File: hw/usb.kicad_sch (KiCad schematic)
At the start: 12 parts, among them J1001 USB_C_Receptacle_USB2.0_14P, Q1001 CSD18543Q3A, U1001 TPD4S480RUKR, U1002 TPS26750SRSMR

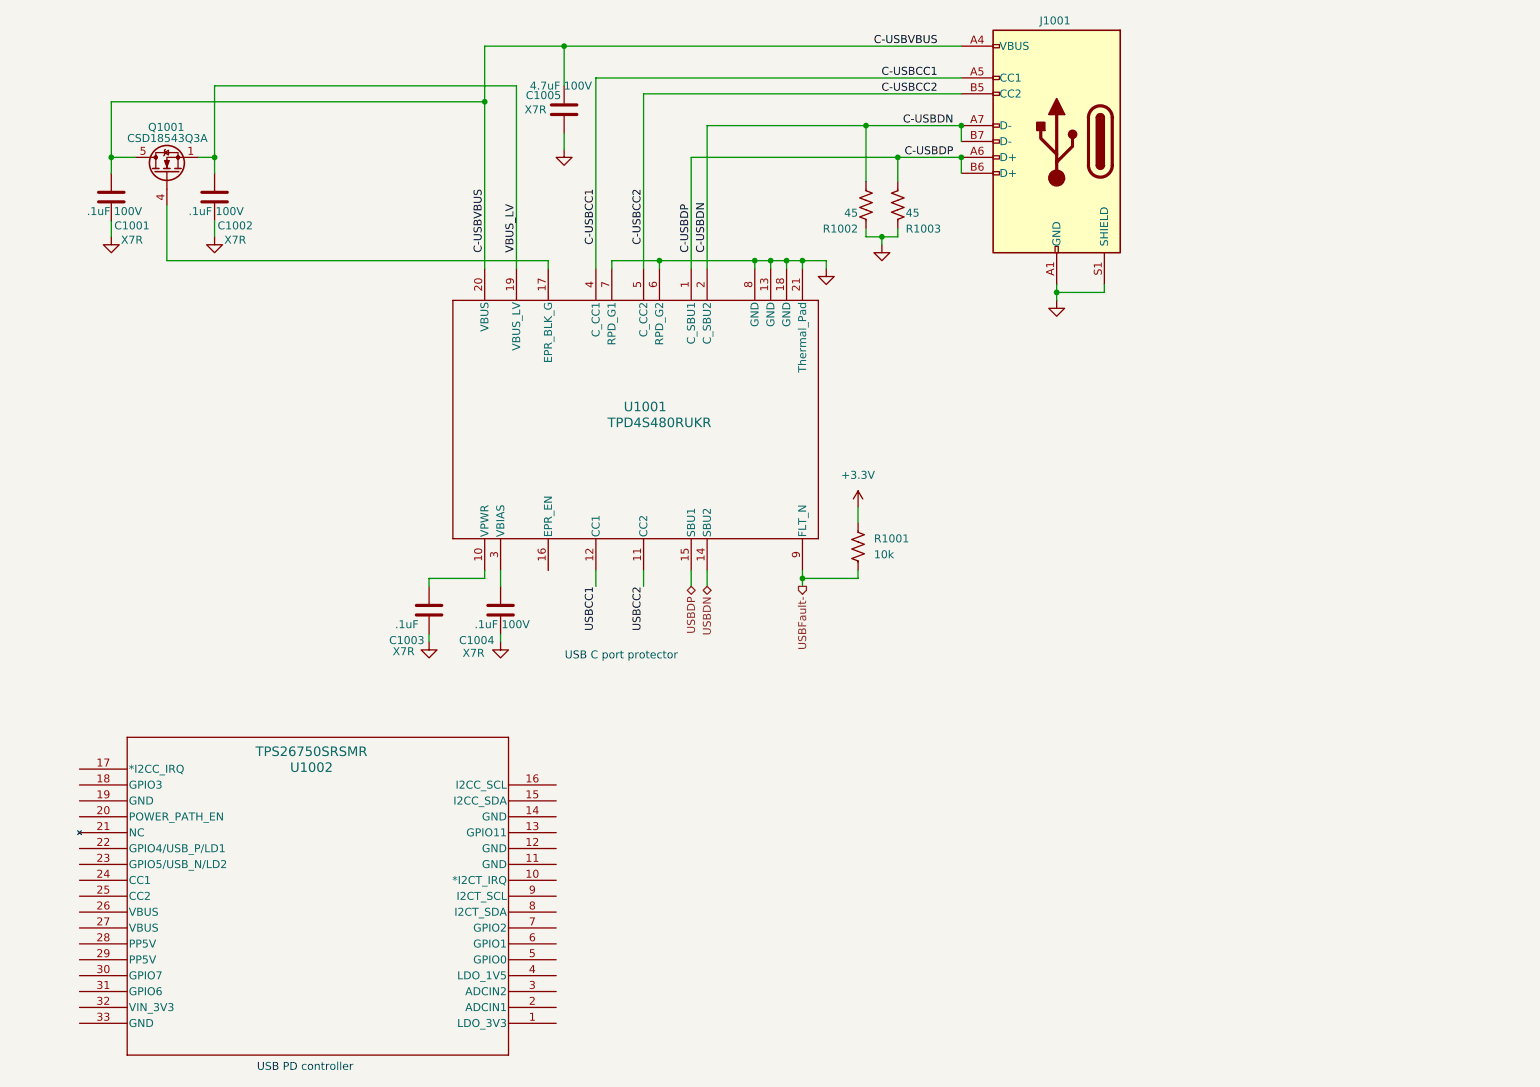
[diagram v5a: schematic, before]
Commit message: Tx LPF and its selection is pretty much done. Fix some OCD. Start to describe the design and construction.
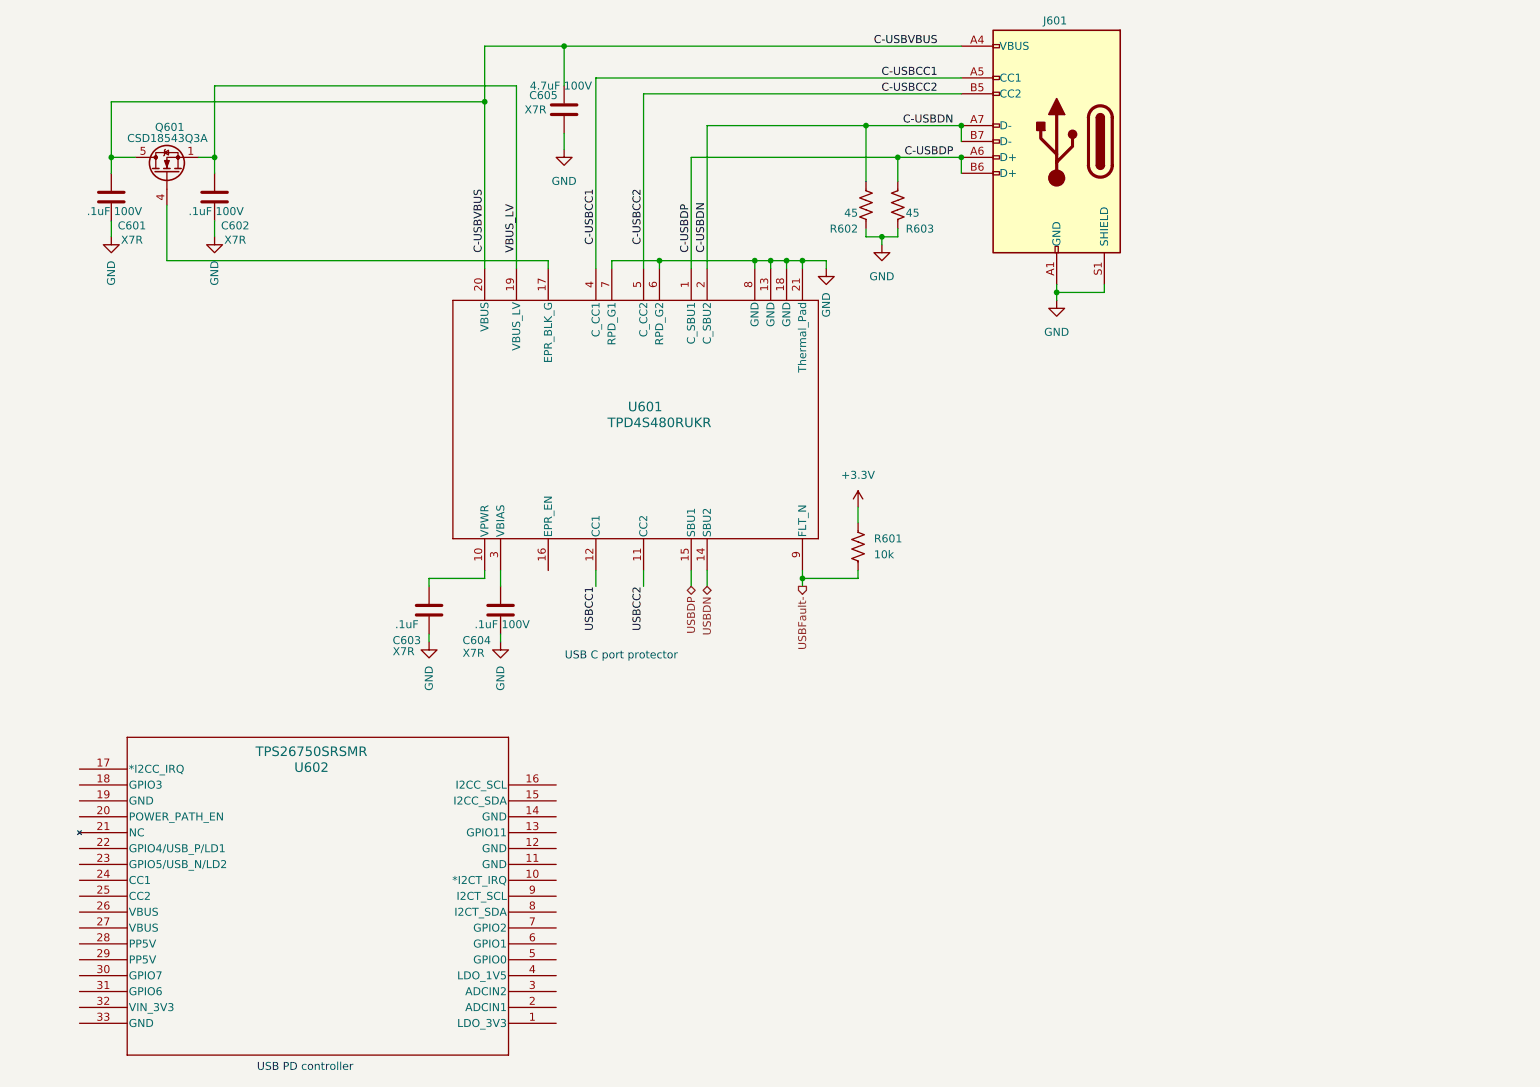
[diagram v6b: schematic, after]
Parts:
- renumbered C1001 to C601, C1002 to C602, C1003 to C603, C1004 to C604, C1005 to C605, J1001 to J601, Q1001 to Q601, R1001 to R601, R1002 to R602, R1003 to R603, U1001 to U601, U1002 to U602
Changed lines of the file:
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@@
 		(on_board yes)
 		(dnp no)
-		(property "Reference" "U1001"
+		(property "Reference" "U601"
 			(at 125.984 84.328 90)
 			(effects
@@
 			(project "USB-SSB-txcvr"
 				(path "/8ae46c04-d01a-4756-8774-512b694bfaff/989674b0-a935-4352-9502-d92e0c9bb54e"
-					(reference "U1001")
+					(reference "U601")
 					(unit 1)
 				)
@@
 		(on_board yes)
 		(dnp no)
-		(property "Reference" "R1003"
+		(property "Reference" "R603"
 			(at 167.64 55.88 0)
 			(effects
@@
 			(project "USB-SSB-txcvr"
 				(path "/8ae46c04-d01a-4756-8774-512b694bfaff/989674b0-a935-4352-9502-d92e0c9bb54e"
-					(reference "R1003")
+					(reference "R603")
 					(unit 1)
 				)
@@
 		(dnp no)
 		(fields_autoplaced yes)
-		(property "Reference" "#PWR01002"
+		(property "Reference" "#PWR0602"
 			(at 57.15 63.5 0)
 			(effects
@@
 				)
 				(justify right)
-				(hide yes)
 			)
 		)
@@
 			(project "USB-SSB-txcvr"
 				(path "/8ae46c04-d01a-4756-8774-512b694bfaff/989674b0-a935-4352-9502-d92e0c9bb54e"
-					(reference "#PWR01002")
+					(reference "#PWR0602")
 					(unit 1)
 				)
@@
 		(dnp no)
 		(fields_autoplaced yes)
-		(property "Reference" "#PWR01008"
+		(property "Reference" "#PWR0608"
 			(at 163.83 64.77 0)
 			(effects
@@
 					(size 1.27 1.27)
 				)
-				(hide yes)
 			)
 		)
@@
 			(project "USB-SSB-txcvr"
 				(path "/8ae46c04-d01a-4756-8774-512b694bfaff/989674b0-a935-4352-9502-d92e0c9bb54e"
-					(reference "#PWR01008")
+					(reference "#PWR0608")
 					(unit 1)
 				)
@@
 		(dnp no)
 		(fields_autoplaced yes)
-		(property "Reference" "#PWR01006"
+		(property "Reference" "#PWR0606"
 			(at 154.94 68.58 0)
 			(effects
@@
 				)
 				(justify right)
-				(hide yes)
 			)
 		)
@@
 			(project "USB-SSB-txcvr"
 				(path "/8ae46c04-d01a-4756-8774-512b694bfaff/989674b0-a935-4352-9502-d92e0c9bb54e"
-					(reference "#PWR01006")
+					(reference "#PWR0606")
 					(unit 1)
 				)
@@
 		(dnp no)
 		(fields_autoplaced yes)
-		(property "Reference" "R1001"
+		(property "Reference" "R601"
 			(at 162.56 105.4099 0)
 			(effects
@@
 			(project ""
 				(path "/8ae46c04-d01a-4756-8774-512b694bfaff/989674b0-a935-4352-9502-d92e0c9bb54e"
-					(reference "R1001")
+					(reference "R601")
 					(unit 1)
 				)
@@
 		(dnp no)
 		(fields_autoplaced yes)
-		(property "Reference" "#PWR01009"
+		(property "Reference" "#PWR0609"
 			(at 191.77 73.66 0)
 			(effects
@@
 					(size 1.27 1.27)
 				)
-				(hide yes)
 			)
 		)
@@
 			(project "USB-SSB-txcvr"
 				(path "/8ae46c04-d01a-4756-8774-512b694bfaff/989674b0-a935-4352-9502-d92e0c9bb54e"
-					(reference "#PWR01009")
+					(reference "#PWR0609")
 					(unit 1)
 				)
@@
 		(on_board yes)
 		(dnp no)
-		(property "Reference" "J1001"
+		(property "Reference" "J601"
 			(at 191.516 22.606 0)
 			(effects
@@
 			(project "USB-SSB-txcvr"
 				(path "/8ae46c04-d01a-4756-8774-512b694bfaff/989674b0-a935-4352-9502-d92e0c9bb54e"
-					(reference "J1001")
+					(reference "J601")
 					(unit 1)
 				)
@@
 		(dnp no)
 		(fields_autoplaced yes)
-		(property "Reference" "#PWR01007"
+		(property "Reference" "#PWR0607"
 			(at 160.02 104.14 0)
 			(effects
@@
 			(project ""
 				(path "/8ae46c04-d01a-4756-8774-512b694bfaff/989674b0-a935-4352-9502-d92e0c9bb54e"
-					(reference "#PWR01007")
+					(reference "#PWR0607")
 					(unit 1)
 				)
@@
 		(dnp no)
 		(fields_autoplaced yes)
-		(property "Reference" "#PWR01005"
+		(property "Reference" "#PWR0605"
 			(at 113.03 49.53 0)
 			(effects
@@
 					(size 1.27 1.27)
 				)
-				(hide yes)
 			)
 		)
@@
 			(project "USB-SSB-txcvr"
 				(path "/8ae46c04-d01a-4756-8774-512b694bfaff/989674b0-a935-4352-9502-d92e0c9bb54e"
-					(reference "#PWR01005")
+					(reference "#PWR0605")
 					(unit 1)
 				)
@@
 		(on_board yes)
 		(dnp no)
-		(property "Reference" "Q1001"
+		(property "Reference" "Q601"
 			(at 52.324 39.624 90)
 			(effects
@@
 			(project "USB-SSB-txcvr"
 				(path "/8ae46c04-d01a-4756-8774-512b694bfaff/989674b0-a935-4352-9502-d92e0c9bb54e"
-					(reference "Q1001")
+					(reference "Q601")
 					(unit 1)
 				)
@@
 		(dnp no)
 		(fields_autoplaced yes)
-		(property "Reference" "#PWR01001"
+		(property "Reference" "#PWR0601"
 			(at 40.64 63.5 0)
 			(effects
@@
 				)
 				(justify right)
-				(hide yes)
 			)
 		)
@@
 			(project "USB-SSB-txcvr"
 				(path "/8ae46c04-d01a-4756-8774-512b694bfaff/989674b0-a935-4352-9502-d92e0c9bb54e"
-					(reference "#PWR01001")
+					(reference "#PWR0601")
 					(unit 1)
 				)
@@
 		(dnp no)
 		(fields_autoplaced yes)
-		(property "Reference" "#PWR01004"
+		(property "Reference" "#PWR0604"
 			(at 102.87 128.27 0)
 			(effects
@@
 				)
 				(justify right)
-				(hide yes)
 			)
 		)
@@
 			(project "USB-SSB-txcvr"
 				(path "/8ae46c04-d01a-4756-8774-512b694bfaff/989674b0-a935-4352-9502-d92e0c9bb54e"
-					(reference "#PWR01004")
+					(reference "#PWR0604")
 					(unit 1)
 				)
@@
 		(dnp no)
 		(fields_autoplaced yes)
-		(property "Reference" "#PWR01003"
+		(property "Reference" "#PWR0603"
 			(at 91.44 128.27 0)
 			(effects
@@
 				)
 				(justify right)
-				(hide yes)
 			)
 		)
@@
 			(project "USB-SSB-txcvr"
 				(path "/8ae46c04-d01a-4756-8774-512b694bfaff/989674b0-a935-4352-9502-d92e0c9bb54e"
-					(reference "#PWR01003")
+					(reference "#PWR0603")
 					(unit 1)
 				)
@@
 		(on_board yes)
 		(dnp no)
-		(property "Reference" "C1002"
+		(property "Reference" "C602"
 			(at 60.452 55.372 0)
 			(effects
@@
 			(project "USB-SSB-txcvr"
 				(path "/8ae46c04-d01a-4756-8774-512b694bfaff/989674b0-a935-4352-9502-d92e0c9bb54e"
-					(reference "C1002")
+					(reference "C602")
 					(unit 1)
 				)
@@
 		(on_board yes)
 		(dnp no)
-		(property "Reference" "R1002"
+		(property "Reference" "R602"
 			(at 160.02 55.88 0)
 			(effects
@@
 			(project "USB-SSB-txcvr"
 				(path "/8ae46c04-d01a-4756-8774-512b694bfaff/989674b0-a935-4352-9502-d92e0c9bb54e"
-					(reference "R1002")
+					(reference "R602")
 					(unit 1)
 				)
@@
 		(on_board yes)
 		(dnp no)
-		(property "Reference" "C1001"
+		(property "Reference" "C601"
 			(at 43.942 55.372 0)
 			(effects
@@
 			(project "USB-SSB-txcvr"
 				(path "/8ae46c04-d01a-4756-8774-512b694bfaff/989674b0-a935-4352-9502-d92e0c9bb54e"
-					(reference "C1001")
+					(reference "C601")
 					(unit 1)
 				)
@@
 		(on_board yes)
 		(dnp no)
-		(property "Reference" "C1004"
+		(property "Reference" "C604"
 			(at 99.06 121.666 0)
 			(effects
@@
 			(project "USB-SSB-txcvr"
 				(path "/8ae46c04-d01a-4756-8774-512b694bfaff/989674b0-a935-4352-9502-d92e0c9bb54e"
-					(reference "C1004")
+					(reference "C604")
 					(unit 1)
 				)
@@
 		(on_board yes)
 		(dnp no)
-		(property "Reference" "C1003"
+		(property "Reference" "C603"
 			(at 87.884 121.666 0)
 			(effects
@@
 			(project "USB-SSB-txcvr"
 				(path "/8ae46c04-d01a-4756-8774-512b694bfaff/989674b0-a935-4352-9502-d92e0c9bb54e"
-					(reference "C1003")
+					(reference "C603")
 					(unit 1)
 				)
@@
 		(on_board yes)
 		(dnp no)
-		(property "Reference" "C1005"
+		(property "Reference" "C605"
 			(at 109.728 34.544 0)
 			(effects
@@
 			(project "USB-SSB-txcvr"
 				(path "/8ae46c04-d01a-4756-8774-512b694bfaff/989674b0-a935-4352-9502-d92e0c9bb54e"
-					(reference "C1005")
+					(reference "C605")
 					(unit 1)
 				)
@@
 		(on_board yes)
 		(dnp no)
-		(property "Reference" "U1002"
+		(property "Reference" "U602"
 			(at 72.644 141.986 0)
 			(effects
@@
 			(project "USB-SSB-txcvr"
 				(path "/8ae46c04-d01a-4756-8774-512b694bfaff/989674b0-a935-4352-9502-d92e0c9bb54e"
-					(reference "U1002")
-					(unit 1)
-				)
+					(reference "U602")
+					(unit 1)
+				)

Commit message: Embarking on a whole new arch for rx without BPFs and using a single digitally tuned tank plus three QSDs to accomplish image rejection in digital domain
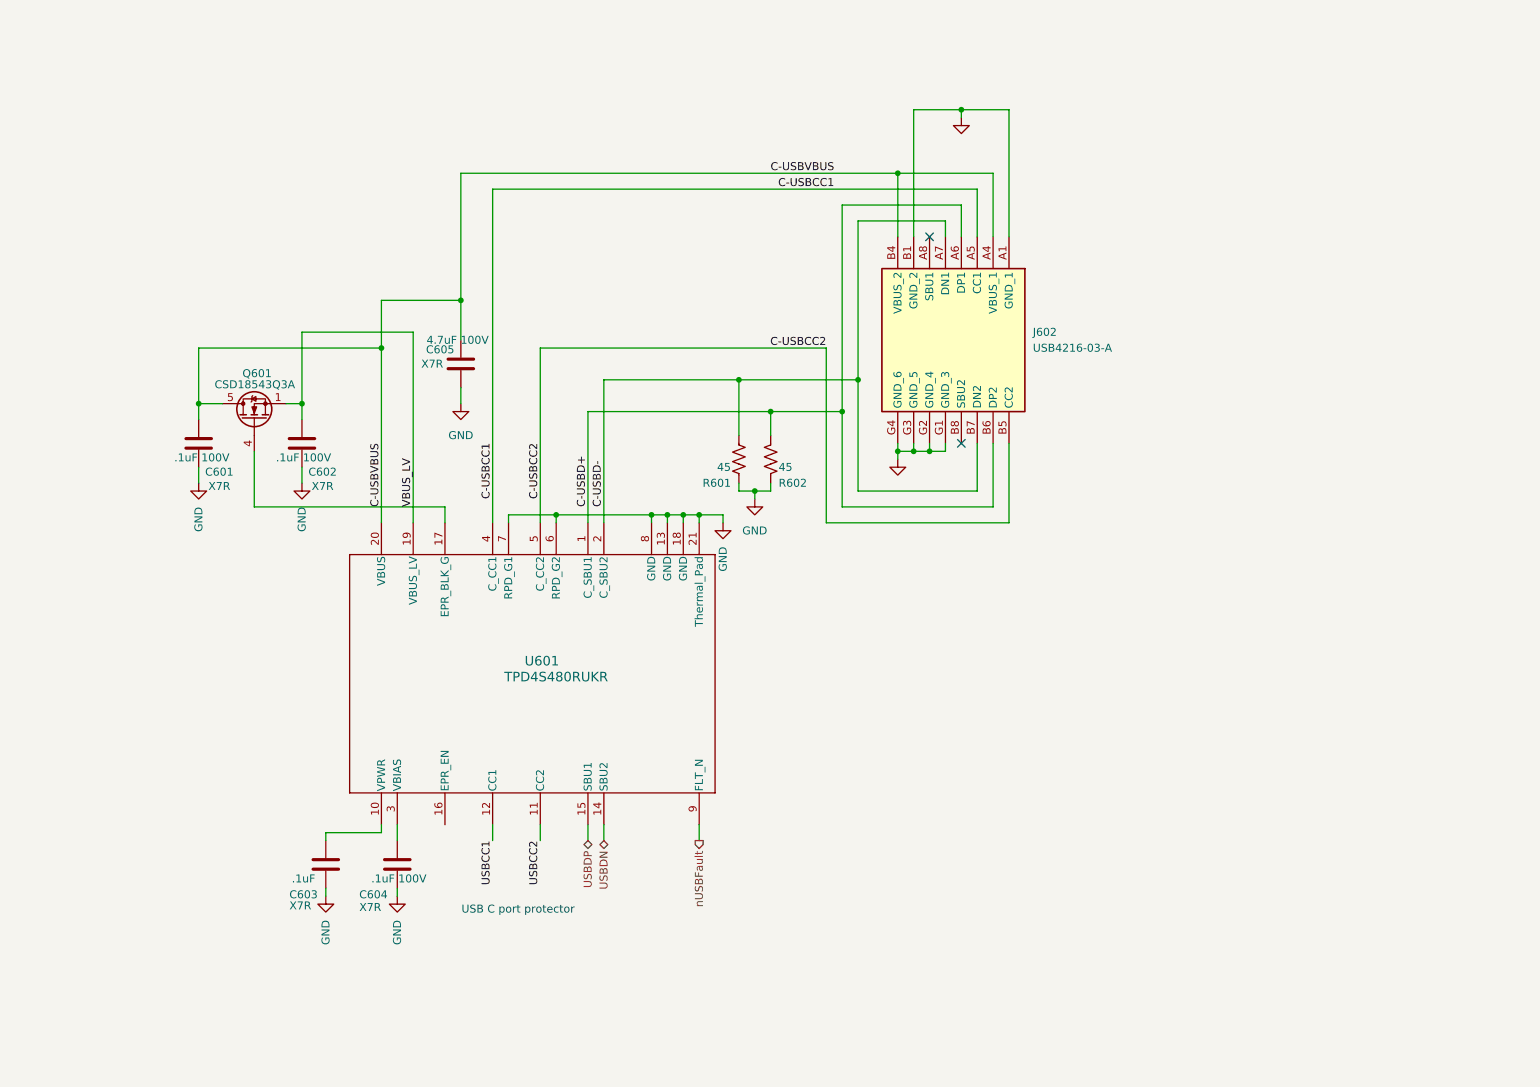
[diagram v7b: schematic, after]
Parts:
- removed J601: USB_C_Receptacle_USB2.0_14P, symbol Connector:USB_C_Receptacle_USB2.0_14P
- removed R601: 10k, symbol Device:R_US
- removed U602: TPS26750SRSMR, VQFN32_RSM_TEX, symbol 2025-03-25_23-54-59:TPS26750SRSMR
- added J602: USB4216-03-A, Library:USB421603A, symbol USB4216-03-A:USB4216-03-A
- C601, C602, C603, C604, C605: footprint (none) -> Capacitor_SMD:C_0805_2012Metric
- U601: footprint RUK0020B-IPC_A -> (none)
- renumbered R602 to R601, R603 to R602
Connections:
- net VBUS_LV is gone; now on net C-USBVBUS: C602.1, Q601.1 (S), Q601.2 (S), Q601.3 (S), U601.19 (VBUS_LV)
- net C-USBCC1: now also J602.A5 (CC1)
- net C-USBCC2: now also J602.B5 (CC2)
- net C-USBVBUS: now also Q601.4 (G), U601.17 (EPR_BLK_G), J602.A4 (VBUS_1), J602.B4 (VBUS_2)
- net GND: now also J602.A1 (GND_1), J602.B1 (GND_2), J602.G1 (GND_3), J602.G2 (GND_4), J602.G3 (GND_5), J602.G4 (GND_6)
- net C-USBDN renamed C-USBD-
- net C-USBD-: now also J602.A7 (DN1), J602.B7 (DN2)
- net C-USBDP renamed C-USBD+
- net C-USBD+: now also J602.A6 (DP1), J602.B6 (DP2)
- net USBFault- renamed nUSBFault
- no-connect marks 0 -> 2
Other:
- note removed: "USB PD controller"
- moved on the sheet: C601, C602, C603, C604, C605, Q601, R601, R602, U601

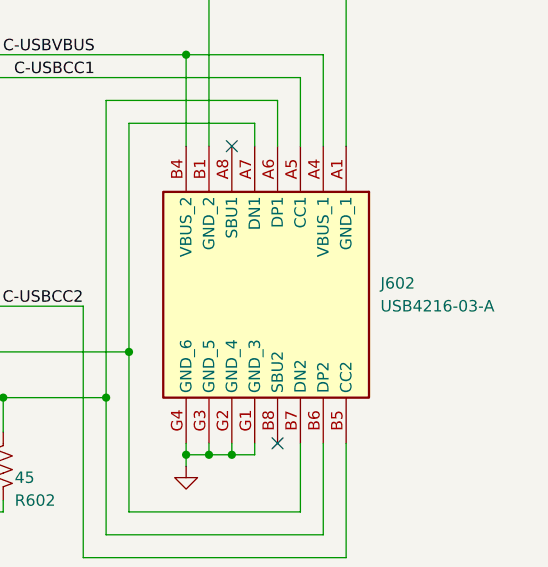
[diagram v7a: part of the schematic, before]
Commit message: Starting to switch to new rx architecture
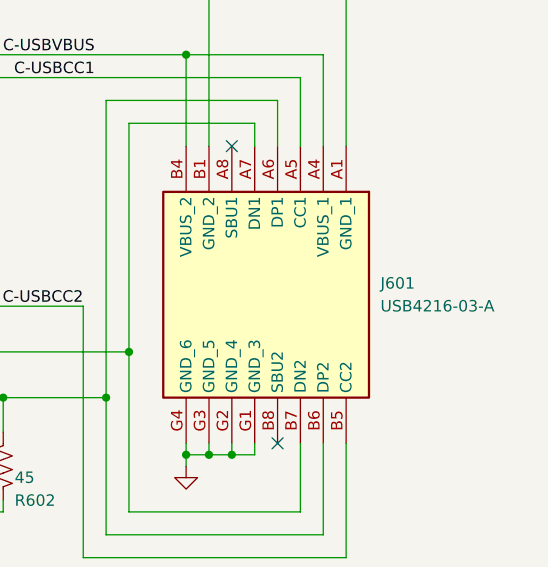
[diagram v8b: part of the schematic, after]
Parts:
- renumbered J602 to J601
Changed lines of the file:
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@@
 		(dnp no)
 		(fields_autoplaced yes)
-		(property "Reference" "#PWR0609"
+		(property "Reference" "#PWR0608"
 			(at 166.37 99.06 0)
 			(effects
@@
 			(project "USB-SSB-txcvr"
 				(path "/8ae46c04-d01a-4756-8774-512b694bfaff/989674b0-a935-4352-9502-d92e0c9bb54e"
-					(reference "#PWR0609")
+					(reference "#PWR0608")
 					(unit 1)
 				)
@@
 		(dnp no)
 		(fields_autoplaced yes)
-		(property "Reference" "#PWR0610"
+		(property "Reference" "#PWR0609"
 			(at 176.53 44.45 0)
 			(effects
@@
 			(project "USB-SSB-txcvr"
 				(path "/8ae46c04-d01a-4756-8774-512b694bfaff/989674b0-a935-4352-9502-d92e0c9bb54e"
-					(reference "#PWR0610")
+					(reference "#PWR0609")
 					(unit 1)
 				)
@@
 		(dnp no)
 		(fields_autoplaced yes)
-		(property "Reference" "J602"
+		(property "Reference" "J601"
 			(at 187.96 72.3899 90)
 			(effects
@@
 			(project ""
 				(path "/8ae46c04-d01a-4756-8774-512b694bfaff/989674b0-a935-4352-9502-d92e0c9bb54e"
-					(reference "J602")
+					(reference "J601")
 					(unit 1)
 				)
